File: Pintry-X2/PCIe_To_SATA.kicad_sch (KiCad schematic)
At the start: 76 parts, among them J10 1735284-3, J9 1735284-3, Q3 BSS138PW, Q4 BSS138PW, U10 SST25VF512A, U11 TPD4EUSB30, U12 TPD4EUSB30, U7 ASM1061, U8 SN74LVC1G17, U9 SN74LVC1G17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

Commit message: Cleaned up schematic
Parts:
- gave numbers to parts that had none: 3
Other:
- note added: "ASM1061 IO"
- note added: "ASM1061 Power"
- note added: "ASM1061 STRAP"
- note added: "Flash"
- note added: "HDD Spin-up control"
- note added: "SATA Connectors"
- moved on the sheet: C18, C19, C20, C21, C22, C23, C24, C25, C26, C27, C28, C29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

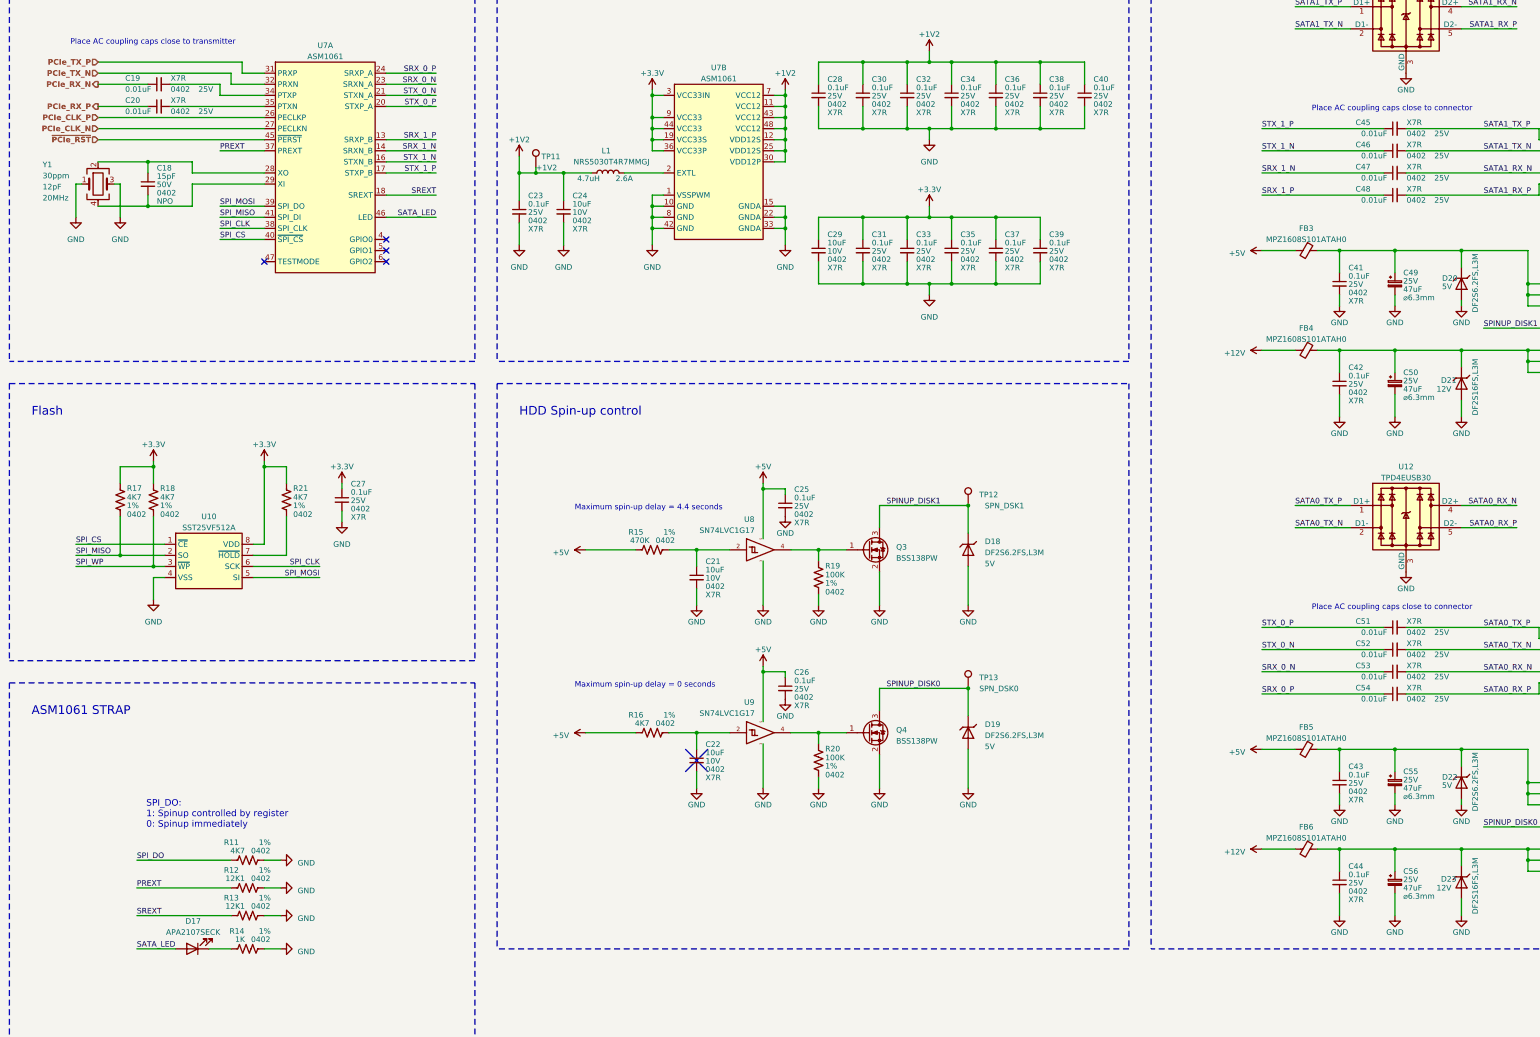
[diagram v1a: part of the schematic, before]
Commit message: Finished Shematic. Starting PCB
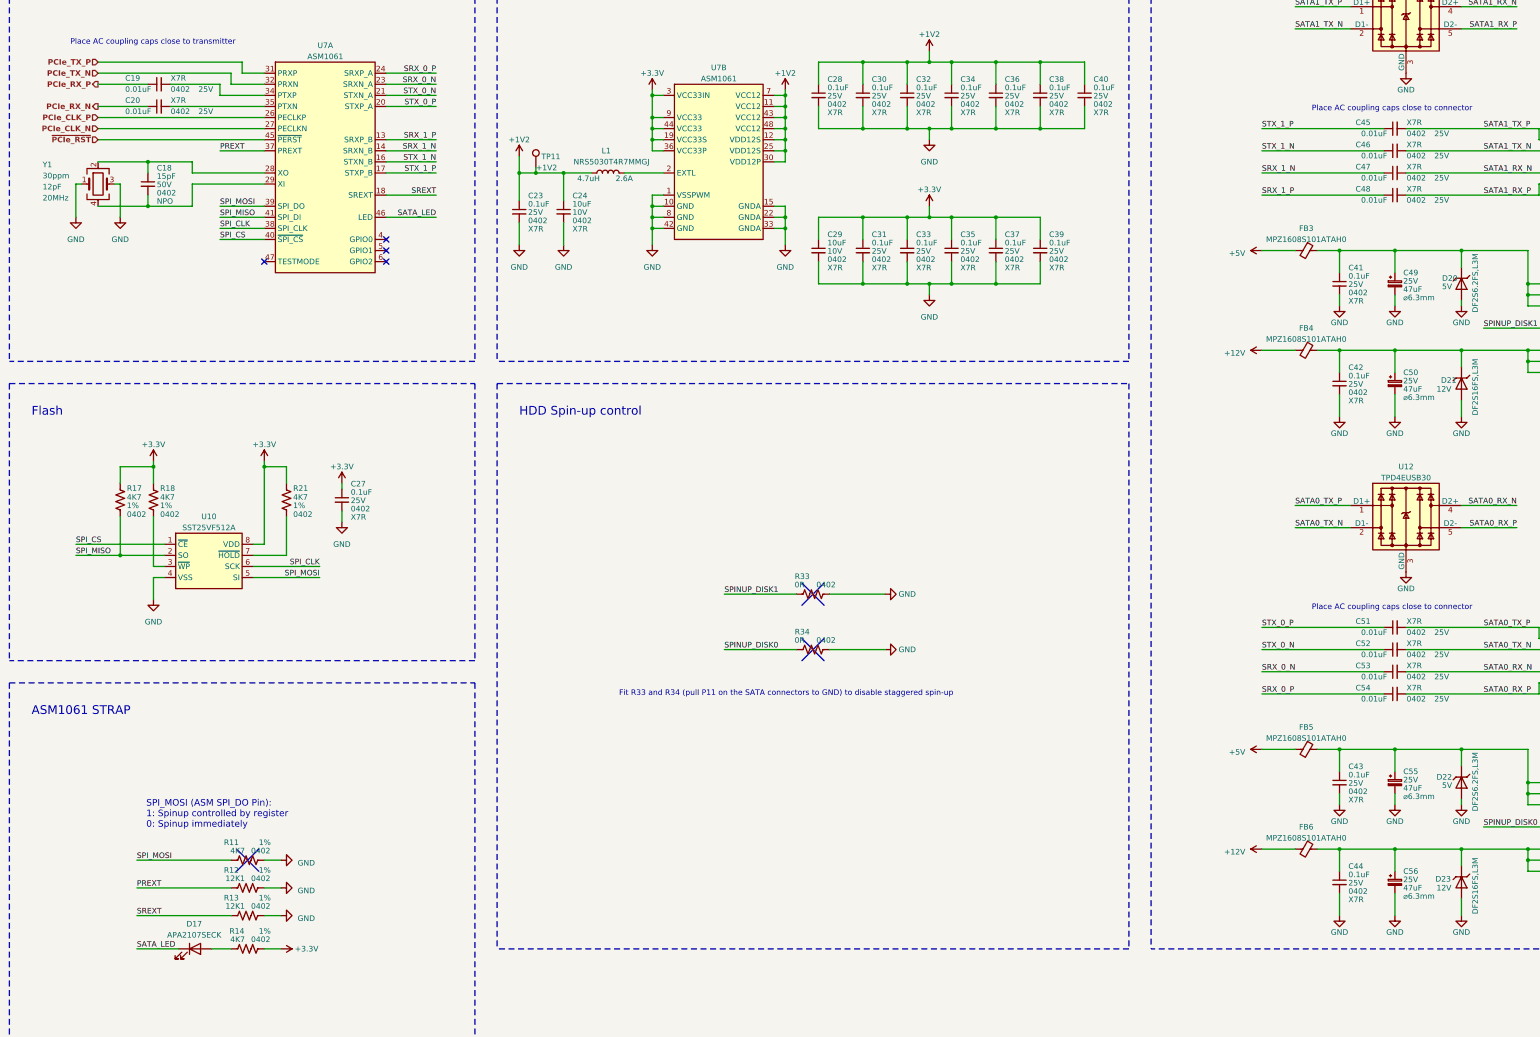
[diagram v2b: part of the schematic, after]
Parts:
- removed C21, C22: 10uF, PintryParts-Footprints:C_0402_1005Metric, symbol Device:C_Small
- removed C25, C26: 0.1uF, PintryParts-Footprints:C_0402_1005Metric, symbol Device:C_Small
- removed D18, D19: DF2S6.2FS,L3M, Diode_SMD:D_SOD-923, symbol PintryParts-Symbols:DF2S6.2FS,L3M
- removed Q3, Q4: BSS138PW, Package_TO_SOT_SMD:SOT-323_SC-70, symbol PintryParts-Symbols:BSS138PW
- removed R15: 470K, PintryParts-Footprints:R_0402_1005Metric, symbol Device:R_US
- removed R16: 4K7, PintryParts-Footprints:R_0402_1005Metric, symbol Device:R_US
- removed R19, R20: 100K, PintryParts-Footprints:R_0402_1005Metric, symbol Device:R_US
- removed TP12: SPN_DSK1, TestPoint:TestPoint_Pad_D2.5mm, symbol Connector:TestPoint
- removed TP13: SPN_DSK0, TestPoint:TestPoint_Pad_D2.5mm, symbol Connector:TestPoint
- removed U8, U9: SN74LVC1G17, Package_TO_SOT_SMD:SOT-23-5, symbol PintryParts-Symbols:SN74LVC1G17
- added R33, R34: 0R, PintryParts-Footprints:R_0402_1005Metric, symbol Device:R_US
- L1: footprint Inductor_SMD:L_Taiyo-Yuden_NR-50xx -> PintryParts-Footprints:L_Taiyo-Yuden_NR-50xx
- R11: fit_field (none) -> dnf
- R14: value 1K -> 4K7
- TP11: footprint TestPoint:TestPoint_Pad_D2.5mm -> TestPoint:TestPoint_Pad_D1.0mm
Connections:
- net SPI_DO is gone; now on net SPI_MOSI: R11.1
- net +3V3: now also R14.2
- net GND: now also R33.2, R34.2; no longer R14.2
- net PCIe_RX_N: now also C20.1; no longer C19.1
- net PCIe_RX_P: now also C19.1; no longer C20.1
- net SATA_LED: now also D17.1 (K); no longer D17.2 (A)
- net SPINUP_DISK0: now also R34.1
- net SPINUP_DISK1: now also R33.1
- net at R14.1: now also D17.2 (A); no longer D17.1 (K)
- net SPI_WP: no longer names the net of R18.2, U10.3 (~WP~)
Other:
- note added: "Fit R33 and R34 (pull P11 on the SATA connectors to GND) to disable staggered spin-up"
- note added: "SPI_MOSI (ASM SPI_DO Pin): 1: Spinup controlled by register 0: Spinup immediately"
- note removed: "Maximum spin-up delay = 0 seconds"
- note removed: "Maximum spin-up delay = 4.4 seconds"
- note removed: "SPI_DO: 1: Spinup controlled by register 0: Spinup immediately"
- moved on the sheet: D17

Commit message: PCB Routing Complete - needs review
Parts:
- TP11: footprint TestPoint:TestPoint_Pad_D1.0mm -> PintryParts-Footprints:TestPoint_Pad_D1.0mm
- U7: Manufacturer (none) -> ASMedia; Part Number (none) -> ASM1061
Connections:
- net GND: now also U7.49 (EP)
- net ~PCIe_RST renamed ~{PCIe_RST}

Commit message: Updated to Rev 1.1. Added interactive HTML
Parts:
- R14: value 4K7 -> 1K
- U10: footprint Package_SO:SOIC-8_5.275x5.275mm_P1.27mm -> Package_SO:SOIC-8_3.9x4.9mm_P1.27mm
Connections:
- net GND: now also Y1.2, Y1.4; no longer Y1.1, Y1.3
- net at C18.1, U7.28 (XO): now also Y1.3; no longer Y1.2
- net at C18.2, U7.29 (XI): now also Y1.1; no longer Y1.4
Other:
- moved on the sheet: Y1
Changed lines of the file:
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@@
   (no_connect (at 373.38 198.12))
   (no_connect (at 373.38 200.66))
-  (wire (pts (xy 33.02 73.66) (xy 34.29 73.66))
-    (stroke (width 0) (type solid) (color 0 0 0 0))
-  )
-  (wire (pts (xy 33.02 81.28) (xy 33.02 73.66))
-    (stroke (width 0) (type solid) (color 0 0 0 0))
+  (wire (pts (xy 33.02 73.66) (xy 33.02 81.28))
+    (stroke (width 0) (type default) (color 0 0 0 0))
   )
   (wire (pts (xy 33.02 156.21) (xy 53.34 156.21))
@@
     (stroke (width 0) (type solid) (color 0 0 0 0))
   )
+  (wire (pts (xy 38.1 68.58) (xy 38.1 69.85))
+    (stroke (width 0) (type default) (color 0 0 0 0))
+  )
   (wire (pts (xy 38.1 68.58) (xy 49.53 68.58))
     (stroke (width 0) (type solid) (color 0 0 0 0))
   )
-  (wire (pts (xy 38.1 78.74) (xy 49.53 78.74))
-    (stroke (width 0) (type solid) (color 0 0 0 0))
+  (wire (pts (xy 38.1 77.47) (xy 38.1 78.74))
+    (stroke (width 0) (type default) (color 0 0 0 0))
   )
-  (wire (pts (xy 41.91 73.66) (xy 43.18 73.66))
+  (wire (pts (xy 38.1 78.74) (xy 49.53 78.74))
     (stroke (width 0) (type solid) (color 0 0 0 0))
   )
@@
       (effects (font (size 1.27 1.27)) (justify left))
     )
-    (property "Value" "4K7" (id 1) (at 71.7549 246.761 90)
+    (property "Value" "1K" (id 1) (at 71.7549 246.761 90)
       (effects (font (size 1.27 1.27)) (justify left))
     )
@@
     (pin "2")
   )
-  (symbol (lib_id "PintryParts-Symbols:ECS-200-12-33-AGN-TR") (at 38.1 73.66 0) (unit 1)
+  (symbol (lib_id "PintryParts-Symbols:ECS-200-12-33-AGN-TR") (at 38.1 73.66 90) (unit 1)
     (in_bom yes) (on_board yes)
-    (property "Reference" "Y1" (id 0) (at 25.4 69.2149 0)
+    (property "Reference" "Y1" (id 0) (at 31.75 69.2149 90)
       (effects (font (size 1.27 1.27)) (justify left))
     )
-    (property "Value" "ECS-200-12-33-AGN-TR" (id 1) (at 40.0049 68.58 0)
+    (property "Value" "ECS-200-12-33-AGN-TR" (id 1) (at 33.02 71.7551 0)
       (effects (font (size 1.27 1.27)) (justify left) hide)
     )
@@
       (effects (font (size 1.27 1.27)) hide)
     )
-    (property "Frequency Stability" "30ppm" (id 6) (at 25.4 71.7549 0)
+    (property "Frequency Stability" "30ppm" (id 6) (at 31.75 71.7549 90)
       (effects (font (size 1.27 1.27)) (justify left))
     )
-    (property "Load Capacitance" "12pF" (id 7) (at 25.4 74.2949 0)
+    (property "Load Capacitance" "12pF" (id 7) (at 31.75 74.2949 90)
       (effects (font (size 1.27 1.27)) (justify left))
     )
-    (property "Frequency" "20MHz" (id 8) (at 25.4 76.8349 0)
+    (property "Frequency" "20MHz" (id 8) (at 31.75 76.8349 90)
       (effects (font (size 1.27 1.27)) (justify left))
     )
@@
     (property "Reference" "U10" (id 0) (at 63.5 149.86 0))
     (property "Value" "SST25VF512A" (id 1) (at 63.5 152.4 0))
-    (property "Footprint" "Package_SO:SOIC-8_5.275x5.275mm_P1.27mm" (id 2) (at 63.5 179.07 0)
+    (property "Footprint" "Package_SO:SOIC-8_3.9x4.9mm_P1.27mm" (id 2) (at 63.5 179.07 0)
       (effects (font (size 1.27 1.27)) hide)
     )
-    (property "Datasheet" "http://ww1.microchip.com/downloads/en/DeviceDoc/20005045C.pdf" (id 3) (at 62.23 147.32 0)
+    (property "Datasheet" "https://ww1.microchip.com/downloads/en/DeviceDoc/25090A.pdf" (id 3) (at 62.23 147.32 0)
       (effects (font (size 1.27 1.27)) hide)
     )
@@
       (effects (font (size 1.27 1.27)) hide)
     )
+    (property "Field6" "" (id 6) (at 63.5 161.29 0))
     (pin "1")
     (pin "2")
